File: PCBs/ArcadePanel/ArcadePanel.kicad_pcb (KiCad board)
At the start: 2 copper layers, 124.5 x 74.9 mm, 52 parts, among them J1 Screw_Terminal_01x10, J10 1, J11 1, J12 1, J13 1, J14 1, J15 1, J16 1, J17 1, J18 1, J19 1, J2 Screw_Terminal_01x10, J20 1, J21 1, J22 1, J23 1, J24 1, J25 1, J26 1, J27 1, J28 1, J29 1, J3 Screw_Terminal_01x12, J30 1, J31 1, J32 1, J33 1, J34 1, J35 1, J36 1, J37 1, J38 1, J39 1, J4 Screw_Terminal_01x12, J40 1, J41 1, J42 1, J43 1, J44 1, J45 1, J46 1, J47 1, J48 1, J5 A1, J6 A2, J7 A3, J8 1, J9 1

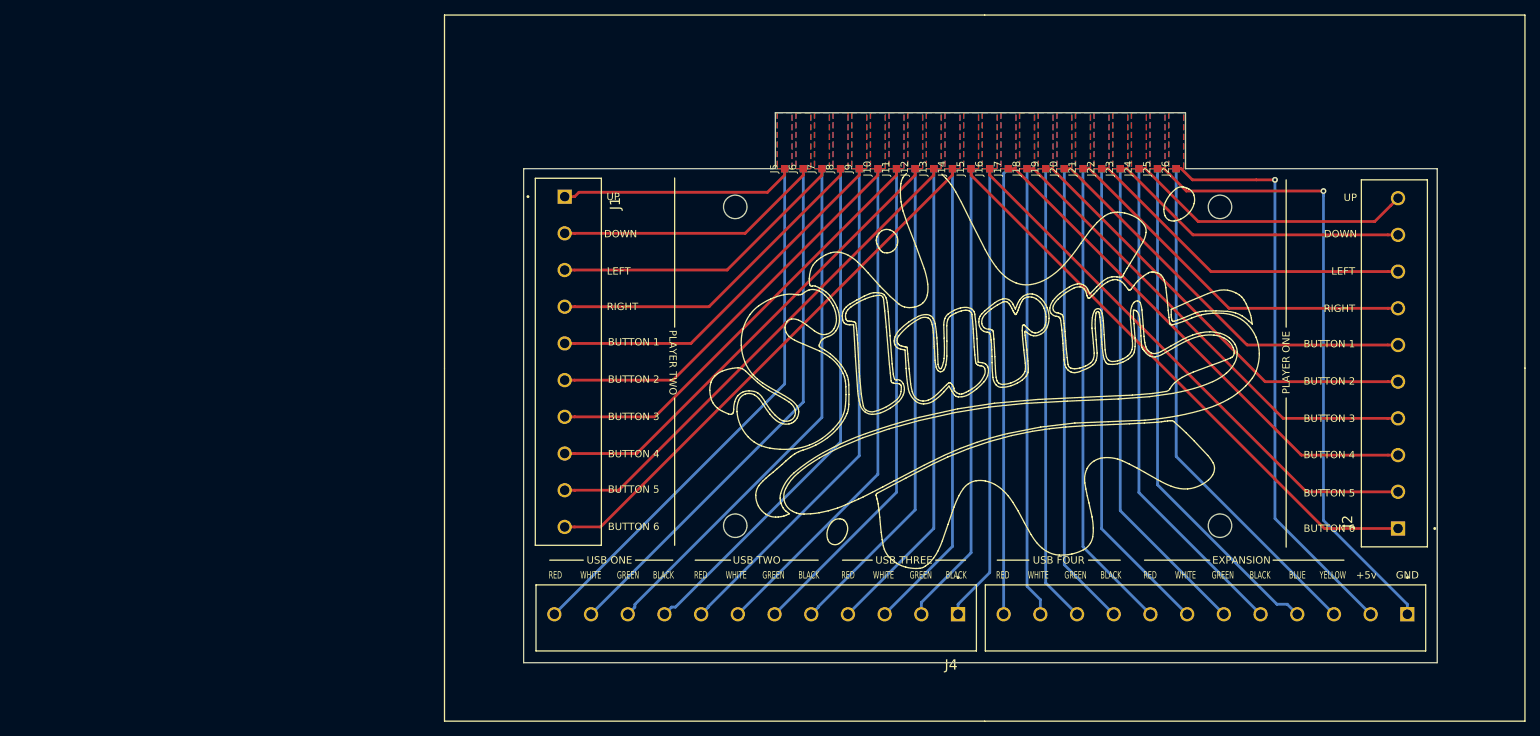
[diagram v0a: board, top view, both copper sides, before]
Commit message: v2 PCB revisions: switch to ribbon cable rather than PCB edge, add DIP switch for panel identifications
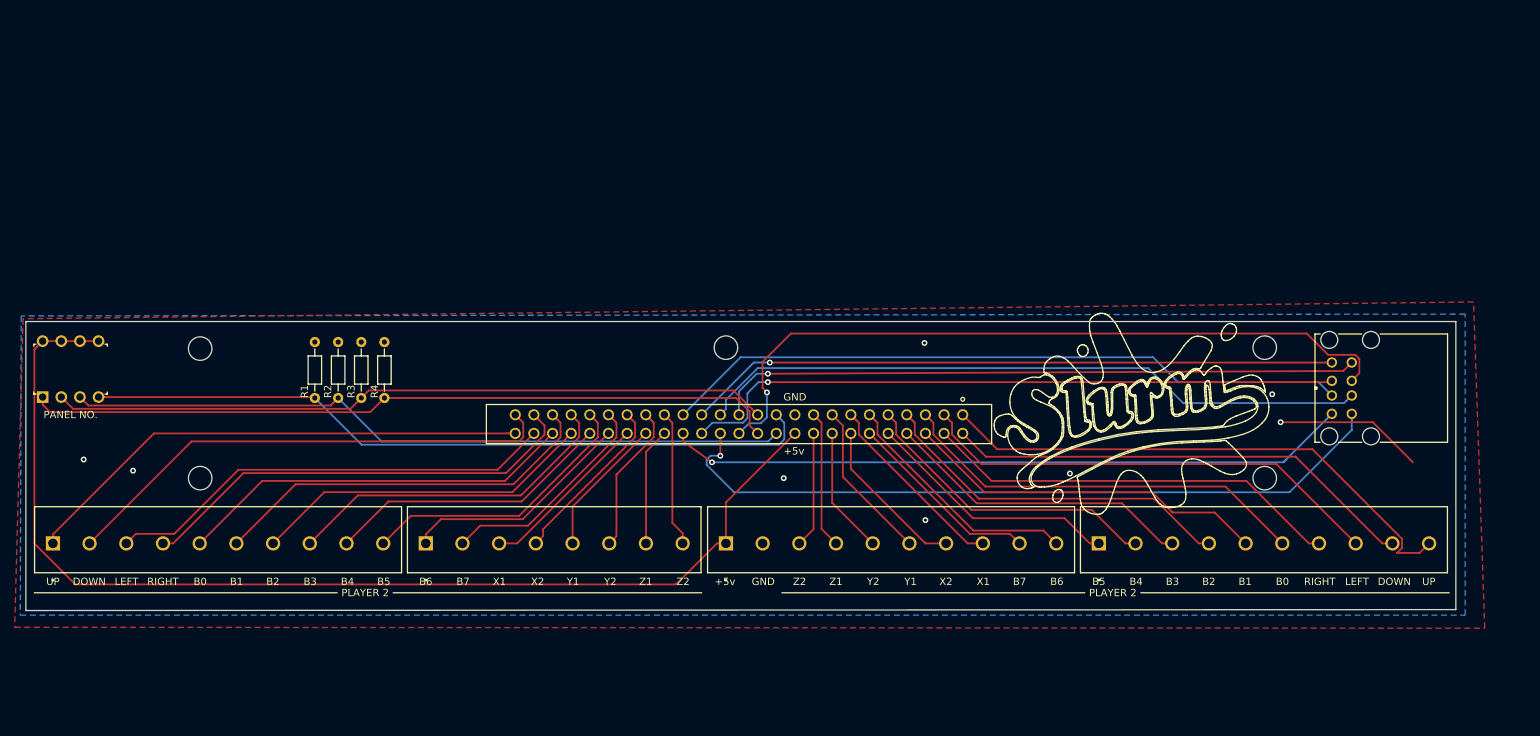
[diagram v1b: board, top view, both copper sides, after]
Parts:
- removed the 4 at (211.7, 109.6)
- removed the 4 at (145.7, 109.6)
- removed the 4 at (211.7, 66.2)
- removed the 4 at (145.7, 66.2)
- removed J10, J11, J12, J13, J14, J15, J16, J17, J18, J19, J20, J21, J22, J23, J24, J25, J26, J27, J28, J29, J30, J31, J32, J33, J34, J35, J36, J37, J38, J39, J40, J41, J42, J43, J44, J45, J46, J47, J48, J8, J9: 1, TestPoint:TestPoint_Pad_1.0x1.0mm-nosilk
- removed J7: A3, TestPoint:TestPoint_Pad_1.0x1.0mm-nosilk
- added 4: MountingHole_3.2mm_M3, MountingHole:MountingHole_3.2mm_M3, F.Cu at (217.8, 103.1)
- added 4: MountingHole_3.2mm_M3, MountingHole:MountingHole_3.2mm_M3, F.Cu at (217.8, 85.3)
- added 4: MountingHole_3.2mm_M3, MountingHole:MountingHole_3.2mm_M3, F.Cu at (144.4, 85.3)
- added 4: MountingHole_3.2mm_M3, MountingHole:MountingHole_3.2mm_M3, F.Cu at (72.8, 103.1)
- added 4: MountingHole_3.2mm_M3, MountingHole:MountingHole_3.2mm_M3, F.Cu at (72.8, 85.5)
- added R1: 10k, Resistor_THT:R_Axial_DIN0204_L3.6mm_D1.6mm_P7.62mm_Horizontal, F.Cu at (88.4, 92.2)
- added R2: 10k, Resistor_THT:R_Axial_DIN0204_L3.6mm_D1.6mm_P7.62mm_Horizontal, F.Cu at (91.6, 92.2)
- added R3: 10k, Resistor_THT:R_Axial_DIN0204_L3.6mm_D1.6mm_P7.62mm_Horizontal, F.Cu at (94.7, 92.2)
- added R4: 10k, Resistor_THT:R_Axial_DIN0204_L3.6mm_D1.6mm_P7.62mm_Horizontal, F.Cu at (97.9, 92.2)
- added SW1: SW_DIP_x04, digikey-footprints:DIP-8_W7.62mm, F.Cu at (51.3, 92.1)
- J3: value Screw_Terminal_01x12 -> SBH11-PBPC-D25-ST-BK; footprint TB001-500-12BE:CUI_TB001-500-12BE -> ul_SBH11PBPCD25STBK:SBH11-PBPC-D25-ST-BK
- J4: value Screw_Terminal_01x12 -> Screw_Terminal_01x08; footprint TB001-500-12BE:CUI_TB001-500-12BE -> TB001-500-08BE:CUI_TB001-500-08BE
- J5: value A1 -> Screw_Terminal_01x10; footprint TestPoint:TestPoint_Pad_1.0x1.0mm-nosilk -> TB001-500-10BE:CUI_TB001-500-10BE
- J6: value A2 -> AU-Y1008-2; footprint TestPoint:TestPoint_Pad_1.0x1.0mm-nosilk -> AU-Y1008-2:AU-Y1008-2
- moved J1 84.2 mm to (52.7, 112.0), turned to 0 degrees
- moved J6 79.4 mm to (226.9, 94.4)
- moved J4 73.2 mm to (103.5, 112.0), turned to 0 degrees
- moved J3 66.4 mm to (176.7, 94.5)
- moved J5 51.7 mm to (144.4, 112.0), turned to 0 degrees
- moved J2 40.8 mm to (195.2, 112.0), turned to 0 degrees
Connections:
- J1 pad 1: Net-(J1-Pad1) -> /P2-UP
- J1 pad 10: Net-(J1-Pad10) -> /P2-B5
- J1 pad 2: Net-(J1-Pad2) -> /P2-DOWN
- J1 pad 3: Net-(J1-Pad3) -> /P2-LEFT
- J1 pad 4: Net-(J1-Pad4) -> /P2-RIGHT
- J1 pad 5: Net-(J1-Pad5) -> /P2-B0
- J1 pad 6: Net-(J1-Pad6) -> /P2-B1
- J1 pad 7: Net-(J1-Pad7) -> /P2-B2
- J1 pad 8: Net-(J1-Pad8) -> /P2-B3
- J1 pad 9: Net-(J1-Pad9) -> /P2-B4
- J2 pad 1: Net-(J15-Pad1) -> /P1-B5
- J2 pad 10: Net-(J2-Pad10) -> /P1-UP
- J2 pad 2: Net-(J16-Pad1) -> /P1-B4
- J2 pad 3: Net-(J17-Pad1) -> /P1-B3
- J2 pad 4: Net-(J18-Pad1) -> /P1-B2
- J2 pad 5: Net-(J19-Pad1) -> /P1-B1
- J2 pad 6: Net-(J2-Pad6) -> /P1-B0
- J2 pad 7: Net-(J2-Pad7) -> /P1-RIGHT
- J2 pad 8: Net-(J2-Pad8) -> /P1-LEFT
- J2 pad 9: Net-(J2-Pad9) -> /P1-DOWN
- J3 pad 1: Net-(J25-Pad1) -> /P1-UP
- J3 pad 10: Net-(J3-Pad10) -> /P1-B5
- J3 pad 11: Net-(J3-Pad11) -> /P1-B6
- J3 pad 12: Net-(J3-Pad12) -> /P1-B7
- J3 pad 2: Net-(J26-Pad1) -> /P1-DOWN
- J3 pad 3: Net-(J27-Pad1) -> /P1-LEFT
- J3 pad 4: Net-(J28-Pad1) -> /P1-RIGHT
- J3 pad 5: Net-(J29-Pad1) -> /P1-B0
- J3 pad 6: Net-(J3-Pad6) -> /P1-B1
- J3 pad 7: Net-(J3-Pad7) -> /P1-B2
- J3 pad 8: Net-(J3-Pad8) -> /P1-B3
- J3 pad 9: Net-(J3-Pad9) -> /P1-B4
- J4 pad 1: Net-(J37-Pad1) -> /P2-B6
- J4 pad 2: Net-(J38-Pad1) -> /P2-B7
- J4 pad 3: Net-(J39-Pad1) -> /P2-X1
- J4 pad 4: Net-(J4-Pad4) -> /P2-X2
- J4 pad 5: Net-(J4-Pad5) -> /P2-Y1
- J4 pad 6: Net-(J4-Pad6) -> /P2-Y2
- J4 pad 7: Net-(J4-Pad7) -> /P2-Z1
- J4 pad 8: Net-(J4-Pad8) -> /P2-Z2
- J5 pad 1: Net-(J1-Pad1) -> /+5v
- J6 pad 1: Net-(J1-Pad2) -> Net-(J3-Pad32)
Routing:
- net /+5v: track 0.00 -> 153.4 mm
- net Net-(J3-Pad24): track 0.00 -> 102.8 mm
- net Net-(J3-Pad28): track 0.00 -> 101.0 mm, vias 0 -> 1
- net Net-(J3-Pad26): track 0.00 -> 100.3 mm, vias 0 -> 1
- net Net-(J3-Pad21): track 0.00 -> 100.2 mm
- net Net-(J3-Pad22): track 0.00 -> 98.7 mm
- net Net-(J3-Pad23): track 0.00 -> 97.9 mm
- net Net-(J3-Pad31): track 0.00 -> 93.8 mm
- net Net-(J3-Pad32): track 0.00 -> 93.6 mm, vias 0 -> 1
- net Net-(J3-Pad27): track 0.00 -> 91.8 mm
- net Net-(J3-Pad30): track 0.00 -> 90.8 mm, vias 0 -> 1
- net Net-(J3-Pad29): track 0.00 -> 88.8 mm, vias 0 -> 1
- net Net-(J3-Pad25): track 0.00 -> 88.1 mm, vias 0 -> 1
- net Net-(J25-Pad1): track 86.3 -> 0.00 mm, vias 1 -> 0
- net Net-(J15-Pad1): track 79.0 -> 0.00 mm
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- added copper zone on B.Cu, net /GND
- added copper zone on F.Cu, net /GND
- removed copper zone on F.Cu, net Net-(J1-Pad1)
- removed copper zone on F.Cu, net Net-(J1-Pad10)
- removed copper zone on F.Cu, net Net-(J1-Pad2)
- removed copper zone on F.Cu, net Net-(J1-Pad3)
- removed copper zone on F.Cu, net Net-(J1-Pad4)
- removed copper zone on F.Cu, net Net-(J1-Pad5)
- removed copper zone on F.Cu, net Net-(J1-Pad6)
- removed copper zone on F.Cu, net Net-(J1-Pad7)
- removed copper zone on F.Cu, net Net-(J1-Pad8)
- removed copper zone on F.Cu, net Net-(J1-Pad9)
- removed copper zone on F.Cu, net Net-(J15-Pad1)
- removed copper zone on F.Cu, net Net-(J16-Pad1)
- removed copper zone on F.Cu, net Net-(J17-Pad1)
- removed copper zone on F.Cu, net Net-(J18-Pad1)
- removed copper zone on F.Cu, net Net-(J19-Pad1)
- removed copper zone on F.Cu, net Net-(J2-Pad10)
- removed copper zone on F.Cu, net Net-(J2-Pad6)
- removed copper zone on F.Cu, net Net-(J2-Pad7)
- removed copper zone on F.Cu, net Net-(J2-Pad8)
- removed copper zone on F.Cu, net Net-(J2-Pad9)
- removed copper zone on F.Cu, net Net-(J25-Pad1)
- removed copper zone on F.Cu, net Net-(J26-Pad1)
- removed copper zone on B.Cu, net Net-(J27-Pad1)
- removed copper zone on B.Cu, net Net-(J28-Pad1)
- removed copper zone on B.Cu, net Net-(J29-Pad1)
- removed copper zone on B.Cu, net Net-(J3-Pad10)
- removed copper zone on B.Cu, net Net-(J3-Pad11)
- removed copper zone on B.Cu, net Net-(J3-Pad12)
- removed copper zone on B.Cu, net Net-(J3-Pad6)
- removed copper zone on B.Cu, net Net-(J3-Pad7)
- removed copper zone on B.Cu, net Net-(J3-Pad8)
- removed copper zone on B.Cu, net Net-(J3-Pad9)
- removed copper zone on B.Cu, net Net-(J37-Pad1)
- removed copper zone on B.Cu, net Net-(J38-Pad1)
- removed copper zone on B.Cu, net Net-(J39-Pad1)
- removed copper zone on B.Cu, net Net-(J4-Pad10)
- removed copper zone on B.Cu, net Net-(J4-Pad11)
- removed copper zone on B.Cu, net Net-(J4-Pad12)
- removed copper zone on B.Cu, net Net-(J4-Pad4)
- removed copper zone on B.Cu, net Net-(J4-Pad5)
- removed copper zone on B.Cu, net Net-(J4-Pad6)
- removed copper zone on B.Cu, net Net-(J4-Pad7)
- removed copper zone on B.Cu, net Net-(J4-Pad8)
- removed copper zone on B.Cu, net Net-(J4-Pad9)
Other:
- board size 124.5 x 74.9 mm -> 194.8 x 39.4 mm
- board text added: "B0"
- board text added: "B1"
- board text added: "B2"
- board text added: "B3"
- board text added: "B4"
- board text added: "B5"
- board text added: "B6"
- board text added: "B7"
- board text added: "BATEMAN - ARCADE CONTROL PANEL v2.0 2020-07"
- board text added: "PANEL NO."
- board text added: "PLAYER 2"
- board text added: "X1"
- board text added: "X2"
- board text added: "Y1"
- board text added: "Y2"
- board text added: "Z1"
- board text added: "Z2"
- board text removed: "BATEMAN - ARCADE CONTROL PANEL v1.0 2020-06"
- board text removed: "BLACK"
- board text removed: "BLUE"
- board text removed: "BUTTON 1"
- board text removed: "BUTTON 2"
- board text removed: "BUTTON 3"
- board text removed: "BUTTON 4"
- board text removed: "BUTTON 5"
- board text removed: "BUTTON 6"
- board text removed: "EXPANSION"
- board text removed: "GREEN"
- board text removed: "Just pop it in there"
- board text removed: "PLAYER ONE"
- board text removed: "PLAYER TWO"
- board text removed: "RED"
- board text removed: "USB FOUR"
- board text removed: "USB ONE"
- board text removed: "USB THREE"
- board text removed: "USB TWO"
- board text removed: "WHITE"
- board text removed: "YELLOW"
